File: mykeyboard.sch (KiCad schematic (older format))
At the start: 19 parts, among them J1 MJ-4PP-9, SW1 SW_PUSH, SW2 SW_PUSH, SW3 SW_PUSH, SW4 SW_PUSH, SW5 SW_PUSH, SW6 SW_PUSH, SW7 SW_PUSH, SW8 SW_PUSH, SW9 SW_PUSH, U1 ProMicro

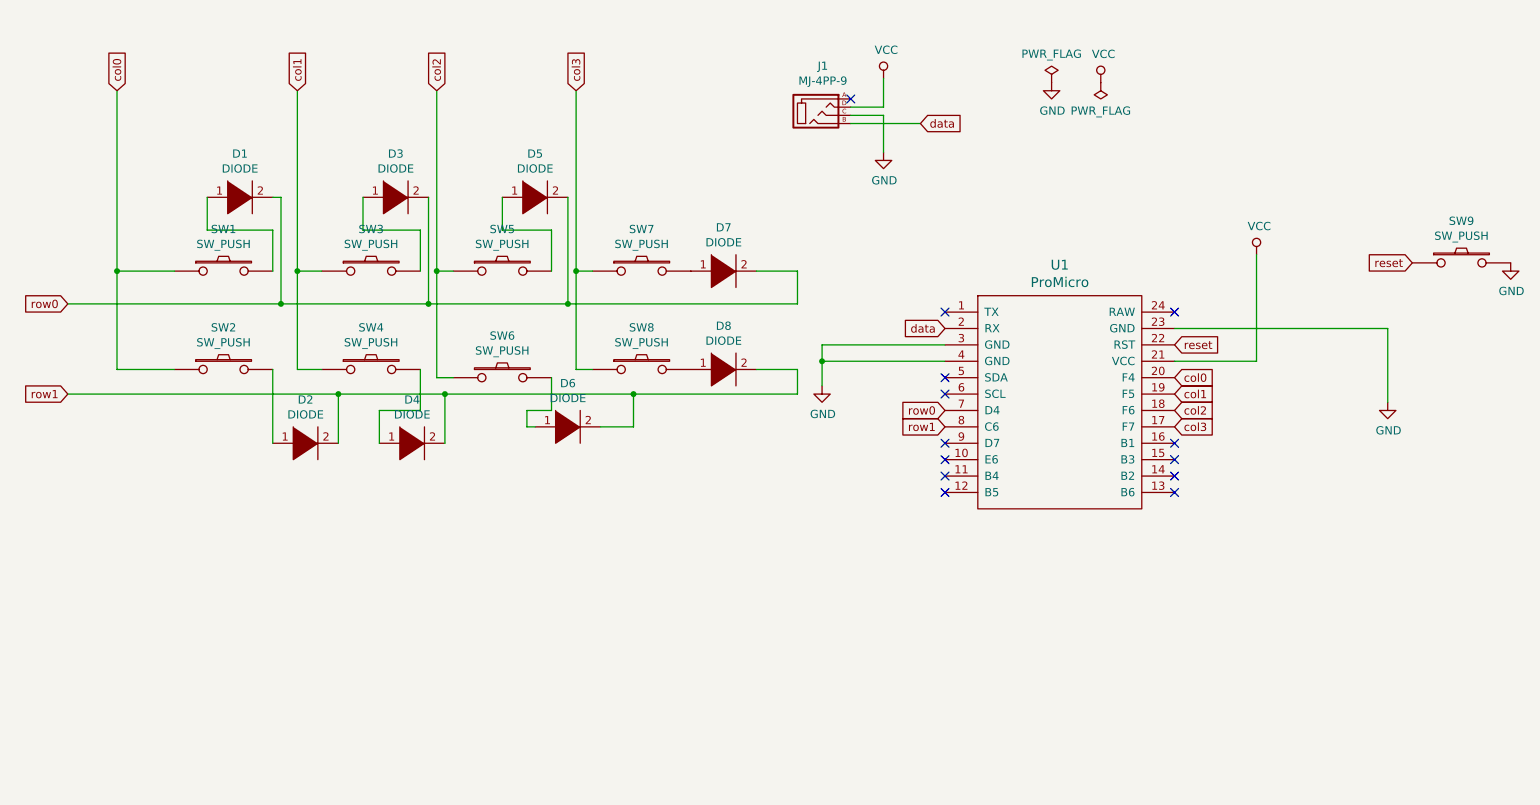
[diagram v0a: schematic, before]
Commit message: LED の回路を設定
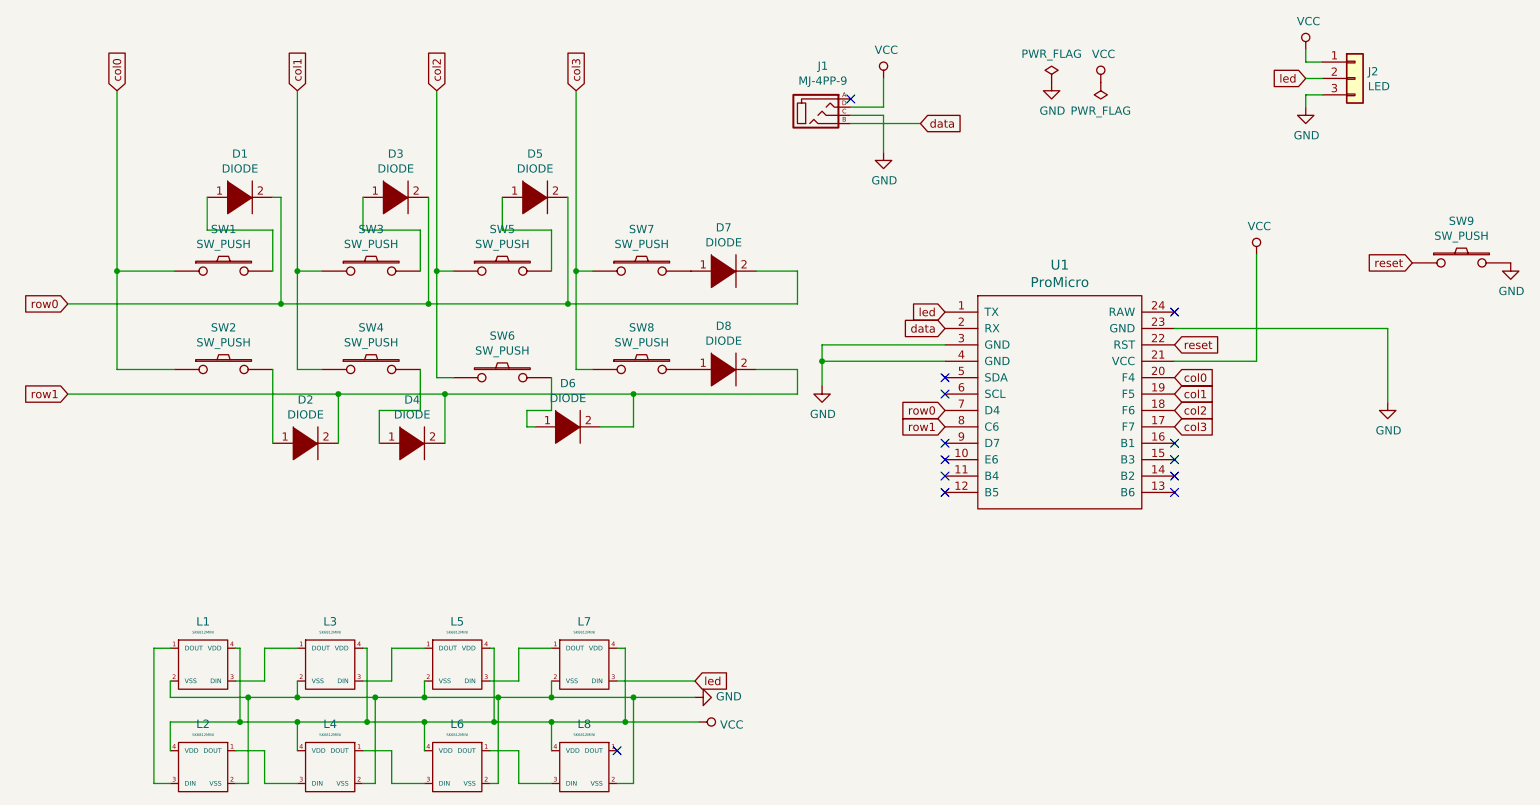
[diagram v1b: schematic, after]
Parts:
- added J2: LED, symbol Connector_Generic:Conn_01x03
- added L1, L2, L3, L4, L5, L6, L7, L8: SK6812MINI, symbol kbd:SK6812MINI
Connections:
- net GND: now also J2.3 (Pin_3), L1.2 (VSS), L2.2 (VSS), L3.2 (VSS), L4.2 (VSS), L5.2 (VSS), L6.2 (VSS), L7.2 (VSS), L8.2 (VSS)
- net VCC: now also J2.1 (Pin_1), L1.4 (VDD), L2.4 (VDD), L3.4 (VDD), L4.4 (VDD), L5.4 (VDD), L6.4 (VDD), L7.4 (VDD), L8.4 (VDD)
- net led: now reaches U1.1 (TX)
- net led: now also J2.2 (Pin_2), L7.3 (DIN)
- new net: L1.1 (DOUT), L2.3 (DIN)
- new net: L1.3 (DIN), L3.1 (DOUT)
- new net: L3.3 (DIN), L5.1 (DOUT)
- new net: L5.3 (DIN), L7.1 (DOUT)
- new net: L2.1 (DOUT), L4.3 (DIN)
- new net: L4.1 (DOUT), L6.3 (DIN)
- new net: L6.1 (DOUT), L8.3 (DIN)

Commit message: フットプリントを定義
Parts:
- D1, D2, D3, D4, D5, D6, D7, D8: footprint kbd:D3_SMD -> kbd:D3_TH_SMD
- J2: footprint (none) -> kbd:StripLED_rev
- L1, L2, L3, L4, L5, L6, L7, L8: footprint (none) -> kbd:SK6812MINI_rev
- SW1, SW2, SW3, SW4, SW5, SW6, SW7, SW8: footprint Keebio-Parts:Hybrid_PCB_100H_Dual_hole-LED -> Keebio-Parts:Hybrid_PCB_100H_Dual_hole
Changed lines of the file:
@@
 F 0 "SW3" H 3050 2805 50  0000 C CNN
 F 1 "SW_PUSH" H 3050 2714 50  0000 C CNN
-F 2 "Keebio-Parts:Hybrid_PCB_100H_Dual_hole-LED" H 3050 2550 50  0001 C CNN
+F 2 "Keebio-Parts:Hybrid_PCB_100H_Dual_hole" H 3050 2550 50  0001 C CNN
 F 3 "" H 3050 2550 50  0000 C CNN
 	1    3050 2550
@@
 F 0 "SW5" H 3850 2805 50  0000 C CNN
 F 1 "SW_PUSH" H 3850 2714 50  0000 C CNN
-F 2 "Keebio-Parts:Hybrid_PCB_100H_Dual_hole-LED" H 3850 2550 50  0001 C CNN
+F 2 "Keebio-Parts:Hybrid_PCB_100H_Dual_hole" H 3850 2550 50  0001 C CNN
 F 3 "" H 3850 2550 50  0000 C CNN
 	1    3850 2550
@@
 F 0 "SW7" H 4700 2805 50  0000 C CNN
 F 1 "SW_PUSH" H 4700 2714 50  0000 C CNN
-F 2 "Keebio-Parts:Hybrid_PCB_100H_Dual_hole-LED" H 4700 2550 50  0001 C CNN
+F 2 "Keebio-Parts:Hybrid_PCB_100H_Dual_hole" H 4700 2550 50  0001 C CNN
 F 3 "" H 4700 2550 50  0000 C CNN
 	1    4700 2550
@@
 F 0 "SW1" H 2150 2805 50  0000 C CNN
 F 1 "SW_PUSH" H 2150 2714 50  0000 C CNN
-F 2 "Keebio-Parts:Hybrid_PCB_100H_Dual_hole-LED" H 2150 2550 50  0001 C CNN
+F 2 "Keebio-Parts:Hybrid_PCB_100H_Dual_hole" H 2150 2550 50  0001 C CNN
 F 3 "" H 2150 2550 50  0000 C CNN
 	1    2150 2550
@@
 F 0 "SW2" H 2150 3405 50  0000 C CNN
 F 1 "SW_PUSH" H 2150 3314 50  0000 C CNN
-F 2 "Keebio-Parts:Hybrid_PCB_100H_Dual_hole-LED" H 2150 3150 50  0001 C CNN
+F 2 "Keebio-Parts:Hybrid_PCB_100H_Dual_hole" H 2150 3150 50  0001 C CNN
 F 3 "" H 2150 3150 50  0000 C CNN
 	1    2150 3150
@@
 F 0 "SW4" H 3050 3405 50  0000 C CNN
 F 1 "SW_PUSH" H 3050 3314 50  0000 C CNN
-F 2 "Keebio-Parts:Hybrid_PCB_100H_Dual_hole-LED" H 3050 3150 50  0001 C CNN
+F 2 "Keebio-Parts:Hybrid_PCB_100H_Dual_hole" H 3050 3150 50  0001 C CNN
 F 3 "" H 3050 3150 50  0000 C CNN
 	1    3050 3150
@@
 F 0 "SW6" H 3850 3455 50  0000 C CNN
 F 1 "SW_PUSH" H 3850 3364 50  0000 C CNN
-F 2 "Keebio-Parts:Hybrid_PCB_100H_Dual_hole-LED" H 3850 3200 50  0001 C CNN
+F 2 "Keebio-Parts:Hybrid_PCB_100H_Dual_hole" H 3850 3200 50  0001 C CNN
 F 3 "" H 3850 3200 50  0000 C CNN
 	1    3850 3200
@@
 F 0 "SW8" H 4700 3405 50  0000 C CNN
 F 1 "SW_PUSH" H 4700 3314 50  0000 C CNN
-F 2 "Keebio-Parts:Hybrid_PCB_100H_Dual_hole-LED" H 4700 3150 50  0001 C CNN
+F 2 "Keebio-Parts:Hybrid_PCB_100H_Dual_hole" H 4700 3150 50  0001 C CNN
 F 3 "" H 4700 3150 50  0000 C CNN
 	1    4700 3150
@@
 F 0 "D7" H 5200 2815 50  0000 C CNN
 F 1 "DIODE" H 5200 2724 50  0000 C CNN
-F 2 "kbd:D3_SMD" H 5200 2550 50  0001 C CNN
+F 2 "kbd:D3_TH_SMD" H 5200 2550 50  0001 C CNN
 F 3 "~" H 5200 2550 50  0001 C CNN
 	1    5200 2550
@@
 F 0 "D8" H 5200 3415 50  0000 C CNN
 F 1 "DIODE" H 5200 3324 50  0000 C CNN
-F 2 "kbd:D3_SMD" H 5200 3150 50  0001 C CNN
+F 2 "kbd:D3_TH_SMD" H 5200 3150 50  0001 C CNN
 F 3 "~" H 5200 3150 50  0001 C CNN
 	1    5200 3150
@@
 F 0 "D6" H 4250 3765 50  0000 C CNN
 F 1 "DIODE" H 4250 3674 50  0000 C CNN
-F 2 "kbd:D3_SMD" H 4250 3500 50  0001 C CNN
+F 2 "kbd:D3_TH_SMD" H 4250 3500 50  0001 C CNN
 F 3 "~" H 4250 3500 50  0001 C CNN
 	1    4250 3500
@@
 F 0 "D4" H 3300 3865 50  0000 C CNN
 F 1 "DIODE" H 3300 3774 50  0000 C CNN
-F 2 "kbd:D3_SMD" H 3300 3600 50  0001 C CNN
+F 2 "kbd:D3_TH_SMD" H 3300 3600 50  0001 C CNN
 F 3 "~" H 3300 3600 50  0001 C CNN
 	1    3300 3600
@@
 F 0 "D2" H 2650 3865 50  0000 C CNN
 F 1 "DIODE" H 2650 3774 50  0000 C CNN
-F 2 "kbd:D3_SMD" H 2650 3600 50  0001 C CNN
+F 2 "kbd:D3_TH_SMD" H 2650 3600 50  0001 C CNN
 F 3 "~" H 2650 3600 50  0001 C CNN
 	1    2650 3600
@@
 F 0 "D1" H 2250 2365 50  0000 C CNN
 F 1 "DIODE" H 2250 2274 50  0000 C CNN
-F 2 "kbd:D3_SMD" H 2250 2100 50  0001 C CNN
+F 2 "kbd:D3_TH_SMD" H 2250 2100 50  0001 C CNN
 F 3 "~" H 2250 2100 50  0001 C CNN
 	1    2250 2100
@@
 F 0 "D3" H 3200 2365 50  0000 C CNN
 F 1 "DIODE" H 3200 2274 50  0000 C CNN
-F 2 "kbd:D3_SMD" H 3200 2100 50  0001 C CNN
+F 2 "kbd:D3_TH_SMD" H 3200 2100 50  0001 C CNN
 F 3 "~" H 3200 2100 50  0001 C CNN
 	1    3200 2100
@@
 F 0 "D5" H 4050 2365 50  0000 C CNN
 F 1 "DIODE" H 4050 2274 50  0000 C CNN
-F 2 "kbd:D3_SMD" H 4050 2100 50  0001 C CNN
+F 2 "kbd:D3_TH_SMD" H 4050 2100 50  0001 C CNN
 F 3 "~" H 4050 2100 50  0001 C CNN
 	1    4050 2100
@@
 F 0 "L1" H 2025 5212 51  0000 C CNN
 F 1 "SK6812MINI" H 2025 5147 16  0000 C CNN
-F 2 "" H 2025 4950 60  0001 C CNN
+F 2 "kbd:SK6812MINI_rev" H 2025 4950 60  0001 C CNN
 F 3 "" H 2025 4950 60  0001 C CNN
 	1    2025 4950
@@
 F 0 "L3" H 2800 5212 51  0000 C CNN
 F 1 "SK6812MINI" H 2800 5147 16  0000 C CNN
-F 2 "" H 2800 4950 60  0001 C CNN
+F 2 "kbd:SK6812MINI_rev" H 2800 4950 60  0001 C CNN
 F 3 "" H 2800 4950 60  0001 C CNN
 	1    2800 4950
@@
 F 0 "L5" H 3575 5212 51  0000 C CNN
 F 1 "SK6812MINI" H 3575 5147 16  0000 C CNN
-F 2 "" H 3575 4950 60  0001 C CNN
+F 2 "kbd:SK6812MINI_rev" H 3575 4950 60  0001 C CNN
 F 3 "" H 3575 4950 60  0001 C CNN
 	1    3575 4950
@@
 F 0 "L7" H 4350 5212 51  0000 C CNN
 F 1 "SK6812MINI" H 4350 5147 16  0000 C CNN
-F 2 "" H 4350 4950 60  0001 C CNN
+F 2 "kbd:SK6812MINI_rev" H 4350 4950 60  0001 C CNN
 F 3 "" H 4350 4950 60  0001 C CNN
 	1    4350 4950
@@
 F 0 "L2" H 2025 5837 51  0000 C CNN
 F 1 "SK6812MINI" H 2025 5772 16  0000 C CNN
-F 2 "" H 2025 5575 60  0001 C CNN
+F 2 "kbd:SK6812MINI_rev" H 2025 5575 60  0001 C CNN
 F 3 "" H 2025 5575 60  0001 C CNN
 	1    2025 5575
@@
 F 0 "L4" H 2800 5837 51  0000 C CNN
 F 1 "SK6812MINI" H 2800 5772 16  0000 C CNN
-F 2 "" H 2800 5575 60  0001 C CNN
+F 2 "kbd:SK6812MINI_rev" H 2800 5575 60  0001 C CNN
 F 3 "" H 2800 5575 60  0001 C CNN
 	1    2800 5575
@@
 F 0 "L6" H 3575 5837 51  0000 C CNN
 F 1 "SK6812MINI" H 3575 5772 16  0000 C CNN
-F 2 "" H 3575 5575 60  0001 C CNN
+F 2 "kbd:SK6812MINI_rev" H 3575 5575 60  0001 C CNN
 F 3 "" H 3575 5575 60  0001 C CNN
 	1    3575 5575
@@
 F 0 "L8" H 4350 5837 51  0000 C CNN
 F 1 "SK6812MINI" H 4350 5772 16  0000 C CNN
-F 2 "" H 4350 5575 60  0001 C CNN
+F 2 "kbd:SK6812MINI_rev" H 4350 5575 60  0001 C CNN
 F 3 "" H 4350 5575 60  0001 C CNN
 	1    4350 5575
@@
 F 0 "J2" H 9129 1417 50  0000 L CNN
 F 1 "LED" H 9129 1326 50  0000 L CNN
-F 2 "" H 9050 1375 50  0001 C CNN
+F 2 "kbd:StripLED_rev" H 9050 1375 50  0001 C CNN
 F 3 "~" H 9050 1375 50  0001 C CNN
 	1    9050 1375

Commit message: LED を配置、ダイオードの位置を変更
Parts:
- U1: footprint kbd:ProMicro_v2 -> Keebio-Parts:ArduinoProMicro-BackSide
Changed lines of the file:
@@
 F 0 "U1" H 7250 4587 60  0000 C CNN
 F 1 "ProMicro" H 7250 4481 60  0000 C CNN
-F 2 "kbd:ProMicro_v2" H 7350 2500 60  0001 C CNN
+F 2 "Keebio-Parts:ArduinoProMicro-BackSide" H 7350 2500 60  0001 C CNN
 F 3 "" H 7350 2500 60  0000 C CNN
 	1    7250 3550
